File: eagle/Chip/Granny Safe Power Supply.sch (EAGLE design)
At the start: 24 parts, among them Q1 TRANS_NPN-MMBTA42, Q2 BT137-600E, U2 TRIAC_OPTOCOUPLER-MOC3063SM, U3 SFH6206

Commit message: tweaked code and updated eagle sch
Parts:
- removed C16: 470uF, SparkFun-Capacitors:47UF-POLAR-PANASONIC_D-35V-20%
- IC2: value (none) -> LM2576WT
- R14: value 12k -> 10k
- R15: value 360 -> 330
- R16: value 100k -> 10k
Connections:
- removed net N$36: Q2.T2@1, Q2.T2@2, U$1.LINE, U2.T1, XFMR1.1
- new net N$5: Q2.T2@1, Q2.T2@2, U$1.LINE, U2.T1, XFMR1.2
- net GND: no longer C16.-
- net N$3: now also XFMR1.1; no longer XFMR1.2
- net N$51: no longer C16.+

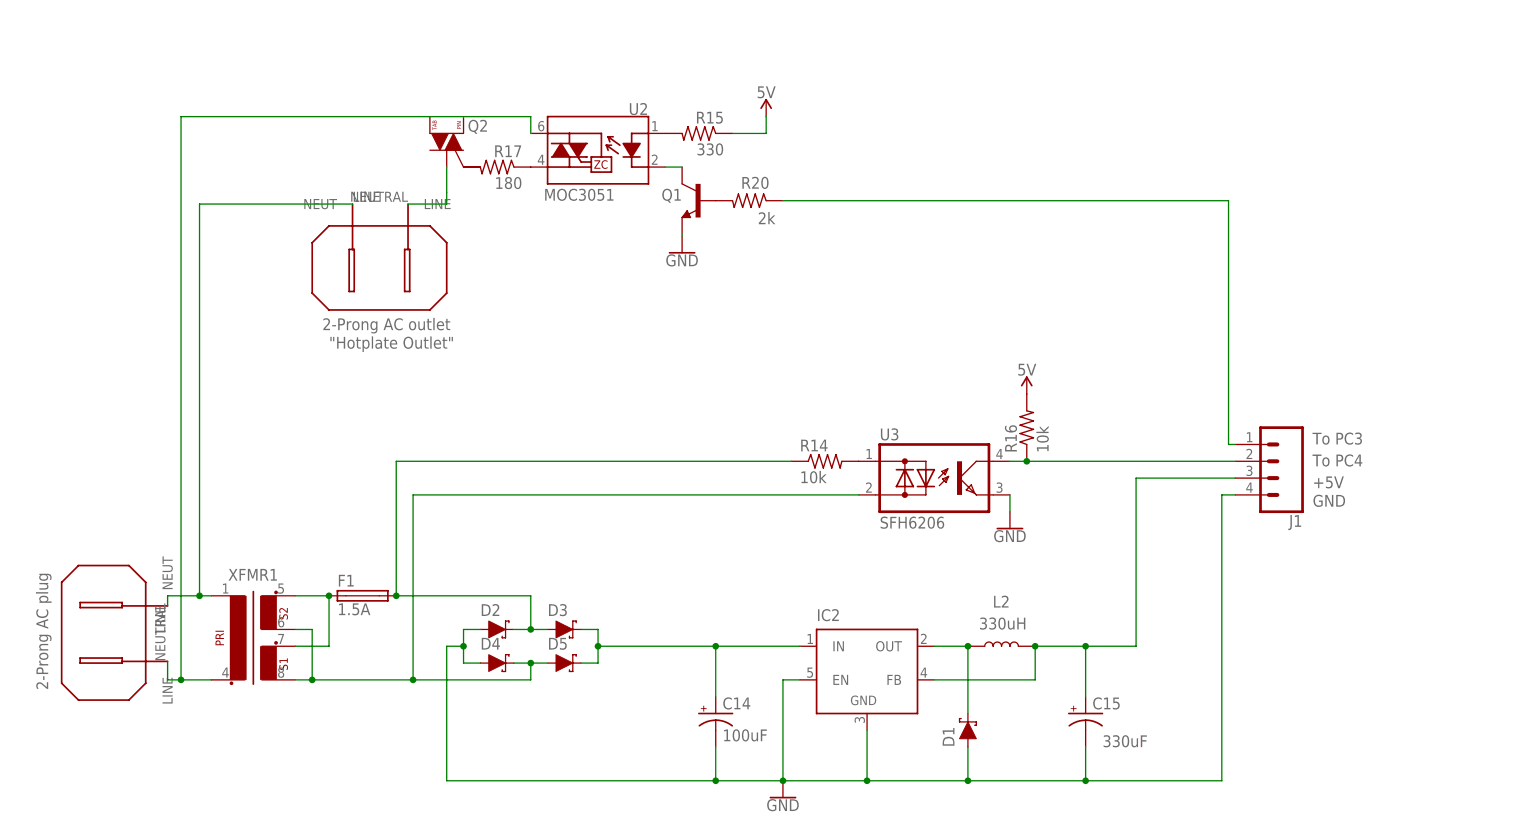
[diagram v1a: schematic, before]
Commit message: update power supply sch.
still need to change the inductor footprint
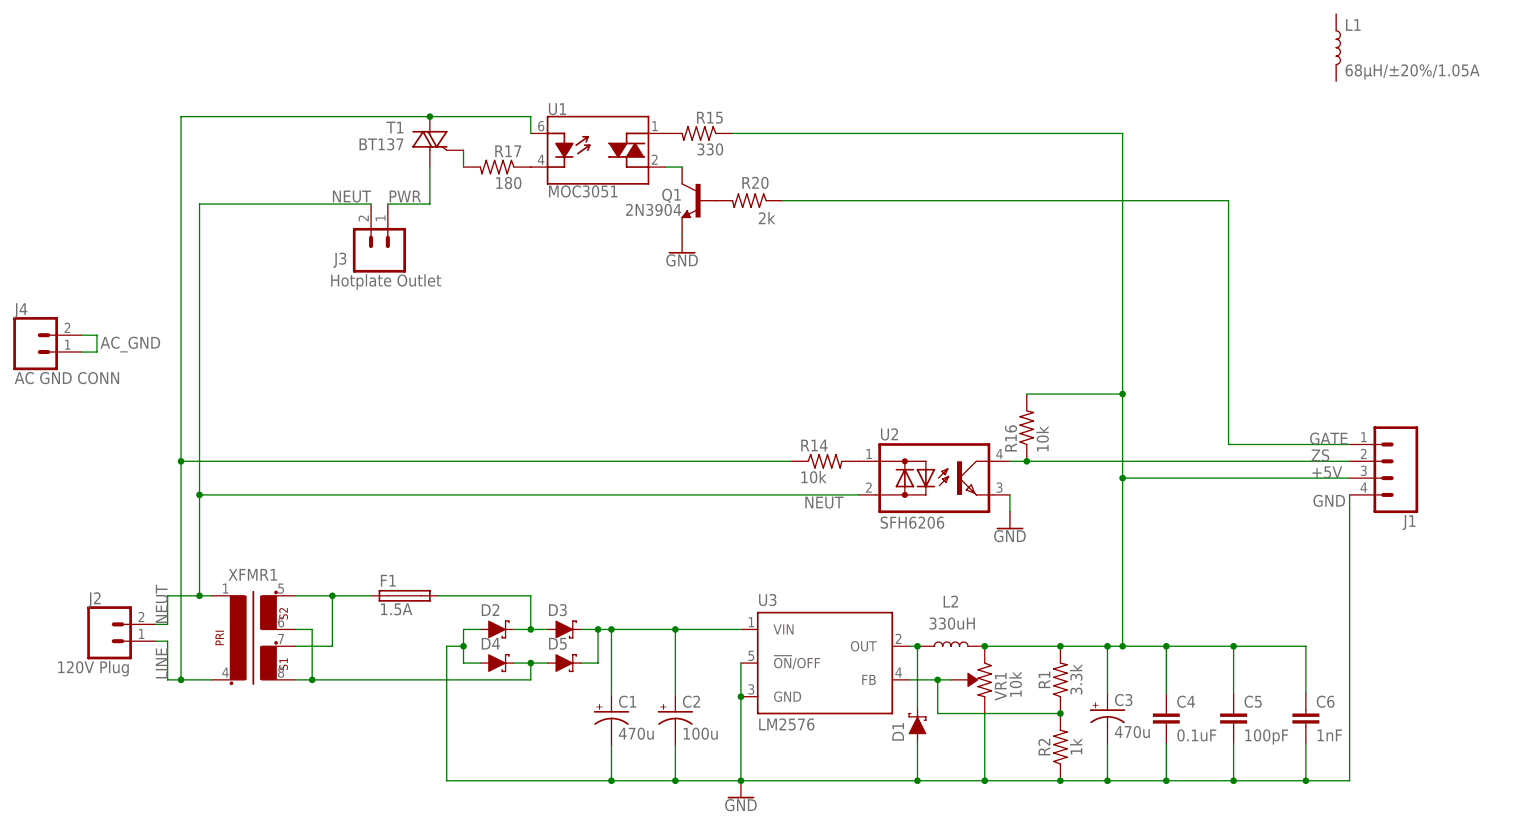
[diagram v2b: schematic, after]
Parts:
- removed C14: 100uF, SparkFun-Capacitors:100UF-POLAR-RADIAL-2.5MM-25V-20%
- removed C15: 47UF-POLAR-PANASONIC_D-50V-20%, SparkFun-Capacitors:47UF-POLAR-PANASONIC_D-50V-20%
- removed IC2: LM2576WT, linear:LM2596TH
- removed Q2: BT137-600E, SparkFun-DiscreteSemi:TRIAC-Z0103MN
- removed U$1, U$2: AC-PLUG, ece:AC-PLUG
- removed U3: SFH6206, optocoupler:SFH6206
- added C1, C3: 470u, adafruit:CPOL-USE5-10.5
- added C2: 100u, adafruit:CPOL-USE5-8.5
- added C4: 0.1uF, SparkFun-Capacitors:0.1UF-0603-25V-5%
- added C5: 100pF, SparkFun-Capacitors:100PF-0603-50V-5%
- added C6: 1nF, SparkFun-Capacitors:1.0NF/1000PF-0603-50V-10%
- added IC1: LM2596S, national-semiconductor:LM2596S
- added J2: 120V Plug, SparkFun-Connectors:CONN_025MM
- added J3: Hotplate Outlet, SparkFun-Connectors:CONN_025MM
- added J4: AC GND CONN, SparkFun-Connectors:CONN_025MM
- added L1: 68µH/±20%/1.05A, SparkFun-Coils:INDUCTOR-CR75-68UH
- added R1: 3.3k, SparkFun-Resistors:3.3KOHM-0603-1/10W-1%
- added R2: 1k, SparkFun-Resistors:1KOHM-0603-1/10W-1%
- added T1: BT137, ece:BT137
- added U1: MOC3051, ece:MOC3051
- added VR1: 10k, SparkFun-Resistors:TRIMPOT-SMD-3MM-OPEN-1/10W-25%
- Q1: value TRANS_NPN-MMBTA42 -> 2N3904
- U2: value TRIAC_OPTOCOUPLER-MOC3063SM -> SFH6206; device SparkFun-DiscreteSemi:TRIAC_OPTOCOUPLER-MOC3063SM -> optocoupler:SFH6206
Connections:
- net N$2 renamed GATE
- removed net 5V: R15.1, R16.2
- removed net N$3: U$1.NEUT, U$2.NEUT, XFMR1.1
- removed net N$30: J1.2, R16.1, U3.C
- removed net N$31: R15.2, U2.A
- removed net N$32: R17.1, U2.T2
- removed net N$37: Q2.T1, U$2.LINE
- removed net N$47: D2.C, D3.A, F1.2, R14.1
- removed net N$5: Q2.T2@1, Q2.T2@2, U$1.LINE, U2.T1, XFMR1.2
- removed net N$52: D4.C, D5.A, U3.AC2, XFMR1.3, XFMR1.5
- new net +5V: C3.+, C4.1, C5.1, C6.1, J1.3, L2.2, R1.2, R15.1, R16.2, VR1.CW
- new net AC_GND: J4.1, J4.2
- new net LINE: J2.1, R14.1, T1.A2, U1.6, XFMR1.2
- new net N$4: D4.C, D5.A, XFMR1.3, XFMR1.5
- new net N$6: D2.C, D3.A, F1.2
- new net N$7: R17.2, T1.G
- new net N$8: R15.2, U1.1
- new net N$9: R17.1, U1.4
- new net NEUT: J2.2, J3.2, U2.AC2, XFMR1.1
- new net PWR: J3.1, T1.A1
- new net ZS: J1.2, R16.1, U2.C
- net GND: now also C1.-, C2.-, C3.-, C4.2, C5.2, C6.2, IC1.!ON!/OFF, IC1.GND, R2.1, U2.E, VR1.CCW; no longer C14.-, C15.-, IC2.EN, IC2.GND, U3.E
- net N$1: now also IC1.FB, R1.1, R2.2, VR1.WIPER; no longer C15.+, IC2.FB, J1.3, L2.2
- net N$29: now also U2.AC1; no longer U3.AC1
- net N$34: now also U1.2; no longer U2.K
- net N$46: now also IC1.OUT; no longer IC2.OUT
- net N$51: now also C1.+, C2.+, IC1.VIN; no longer C14.+, IC2.IN
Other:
- note added: "LM2576"
- note added: "U3"
- note removed: ""Hotplate Outlet""
- note removed: "+5V"
- note removed: "2-Prong AC outlet"
- note removed: "2-Prong AC plug"
- note removed: "330uF"
- note removed: "GND"
- note removed: "MOC3051"
- note removed: "To PC3"
- note removed: "To PC4"
- moved on the sheet: D1, F1, J1, L2

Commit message: Think power supply schematic is ready to go.
Need to decide about XFMR on board or not.
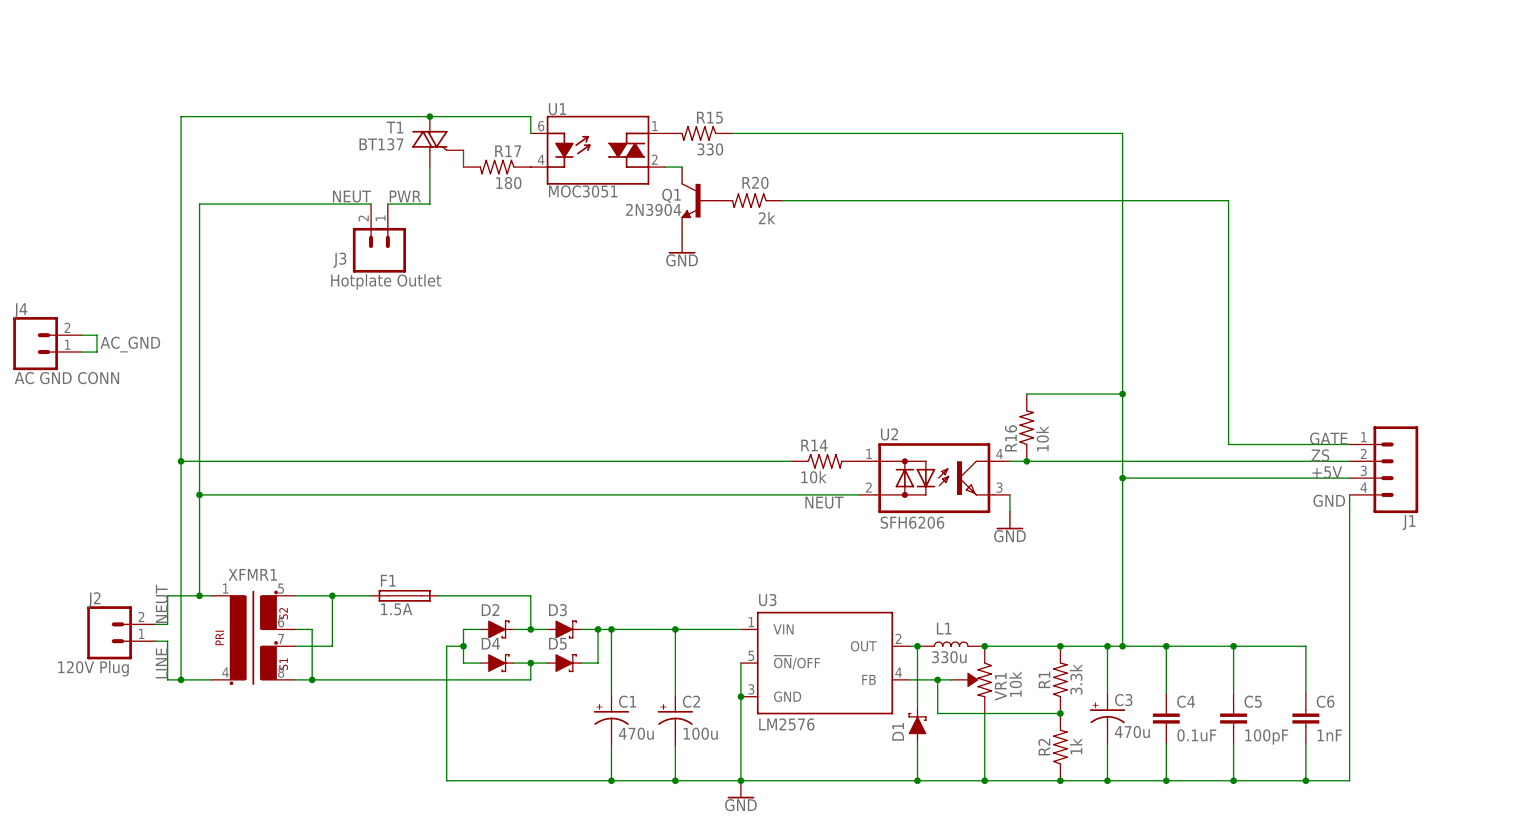
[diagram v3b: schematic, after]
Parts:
- removed L2: 330uH, SparkFun-Coils:INDUCTOR-CR75-68UH
- L1: value 68µH/±20%/1.05A -> INDUCTOR; device SparkFun-Coils:INDUCTOR-CR75-68UH -> ece:INDUCTOR
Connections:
- net +5V: now also L1.2; no longer L2.2
- net N$46: now also L1.1; no longer L2.1
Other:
- note added: "330u"
- moved on the sheet: L1

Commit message: PWR SUP, all but test point
need a way to hook up the resistor too
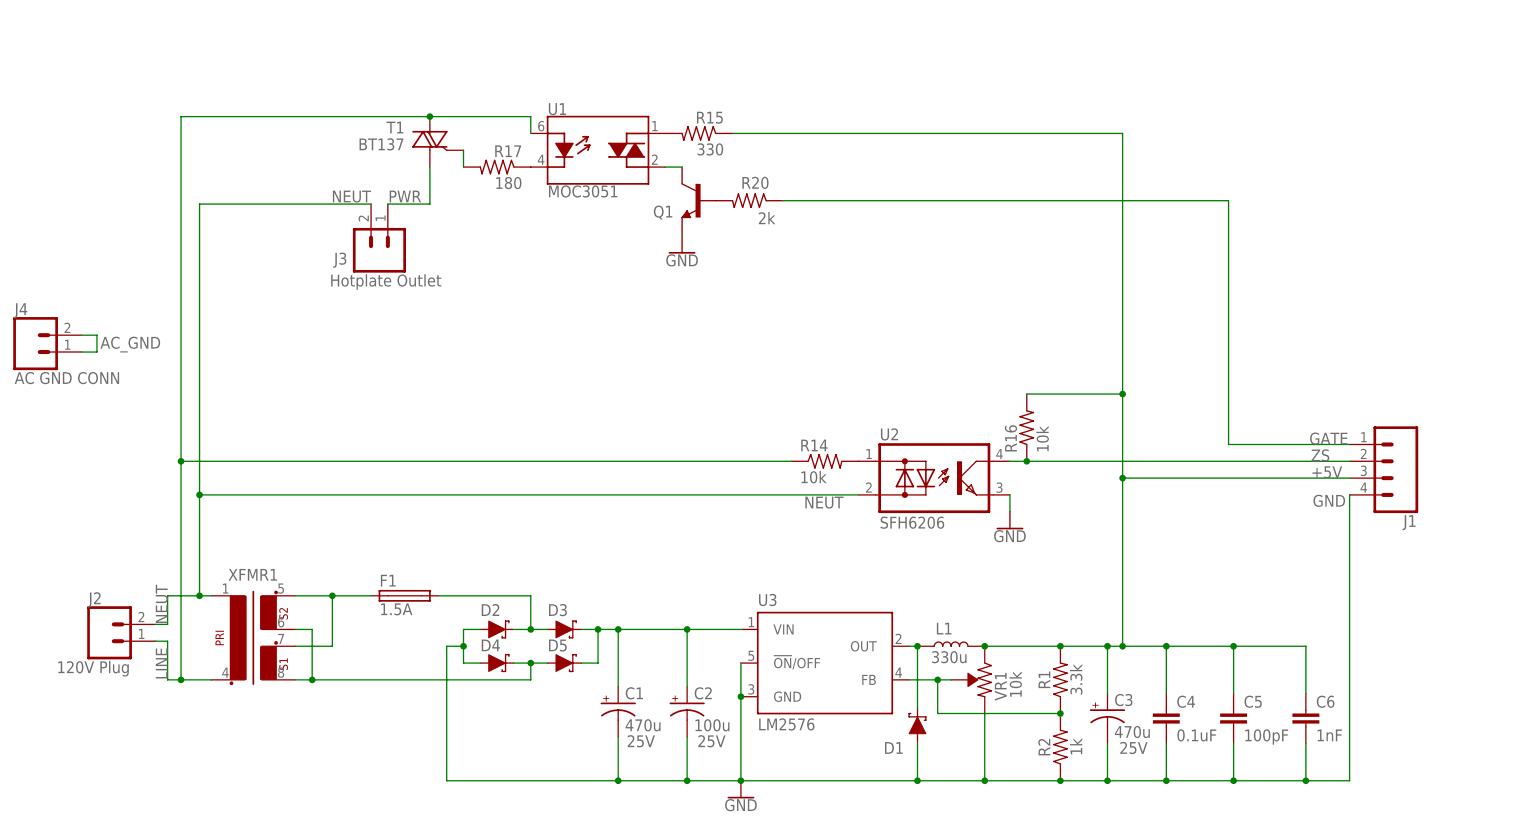
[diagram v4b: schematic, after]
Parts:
- C1, C3: device adafruit:CPOL-USE5-10.5 -> adafruit:CPOL-USE3.5-8
- C2: device adafruit:CPOL-USE5-8.5 -> adafruit:CPOL-USE2-5
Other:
- note added: "25V"
- moved on the sheet: C1, C2
